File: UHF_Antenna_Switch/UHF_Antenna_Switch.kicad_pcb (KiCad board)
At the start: 2 copper layers, 157.2 x 60 mm, 47 parts, among them J1 Conn_N_Type_Female, J2 Conn_SO-239, J3 Conn_SMA_Female, J4 Screw_Terminal_01x04, J5 Conn_02x03_Odd_Even, K1 HF3-51, K2 HF3-51, Q2 2N7002, Q3 2N7002, SW1 SW_SP3T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

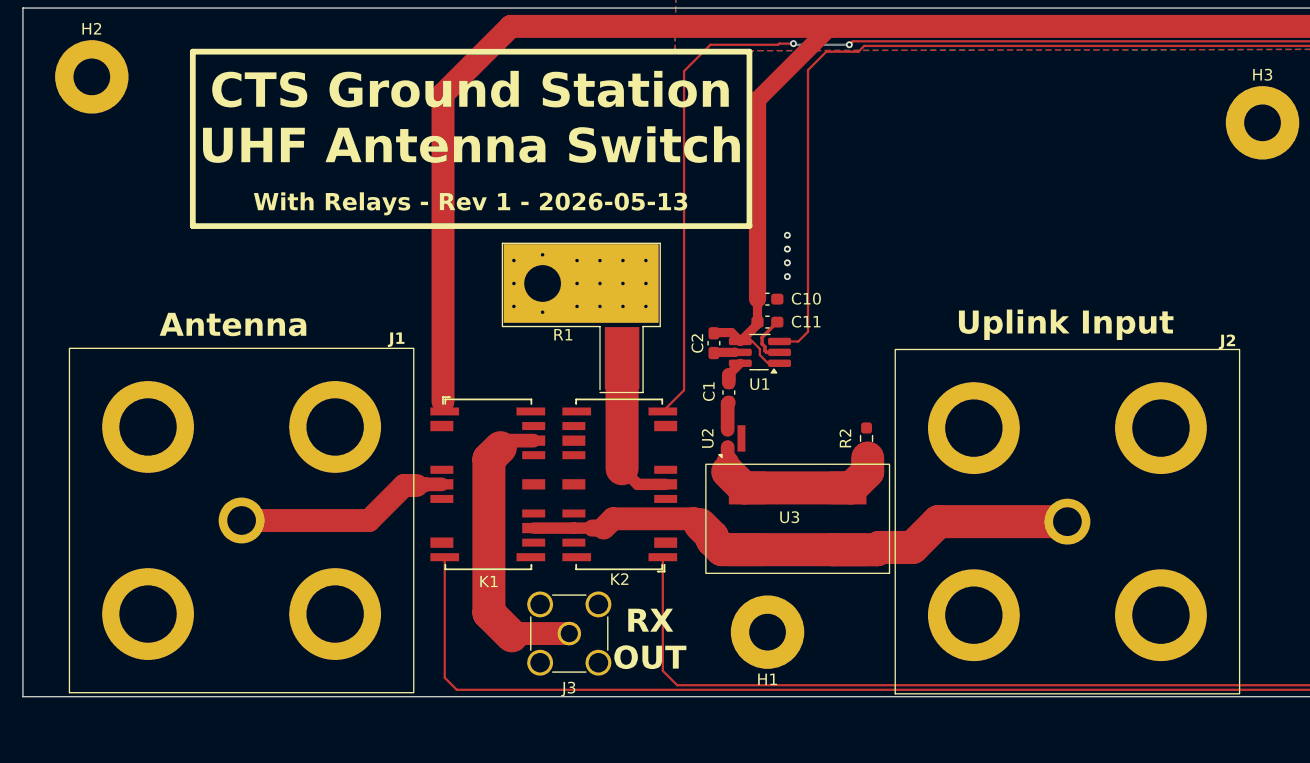
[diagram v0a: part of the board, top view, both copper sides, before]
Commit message: chore(pcb): Minor layout tweaks in RF area
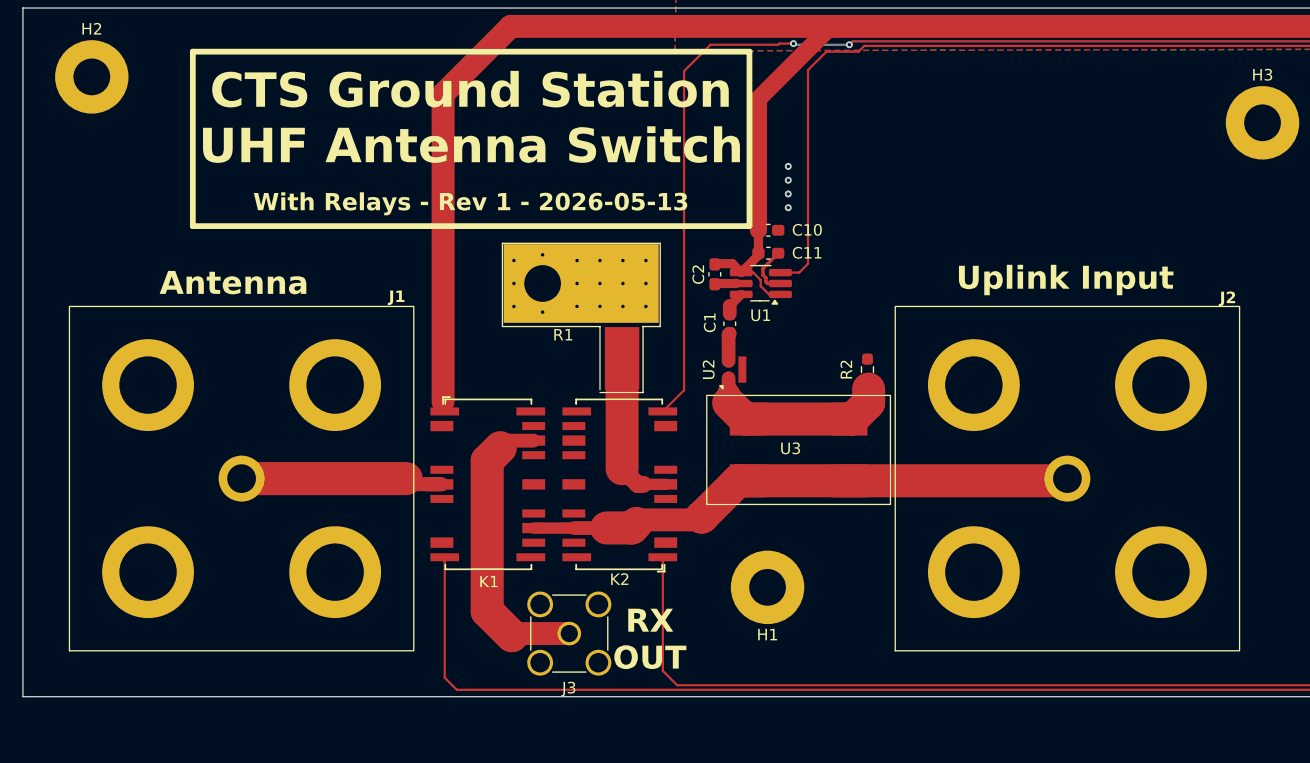
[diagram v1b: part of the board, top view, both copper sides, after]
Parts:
- moved C1 6.00 mm to (136.6, 102.5)
- moved C10 6.00 mm to (139.9, 94.4)
- moved C11 6.00 mm to (139.9, 96.4)
- moved C2 6.00 mm to (135.3, 98.2)
- moved R2 6.00 mm to (148.6, 106.5)
- moved U1 6.00 mm to (139.3, 99.0)
- moved U2 6.00 mm to (137.1, 106.5)
- moved U3 6.00 mm to (142.6, 114.8)
- moved H1 3.90 mm to (139.9, 125.5)
- moved J2 3.75 mm to (166.0, 116.0)
- moved J1 3.65 mm to (94.0, 116.0)
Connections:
- net /Relay_K1/RF_COMMON renamed /RF_PORT_ANT
- net /Relay_K1/RF_NC renamed /RF_PORT_RX
- net Net-(J2-In) renamed /RF_PORT_TX
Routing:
- net TX_DETECTED: track 135.1 -> 129.1 mm
- net +3V3: track 423.7 -> 417.8 mm
- net /RF_PORT_TX: track 21.5 -> 20.5 mm
- net /RF_PORT_ANT: track 18.1 -> 19.1 mm
- net /Relay_K1/RF_NO: track 22.6 -> 21.8 mm

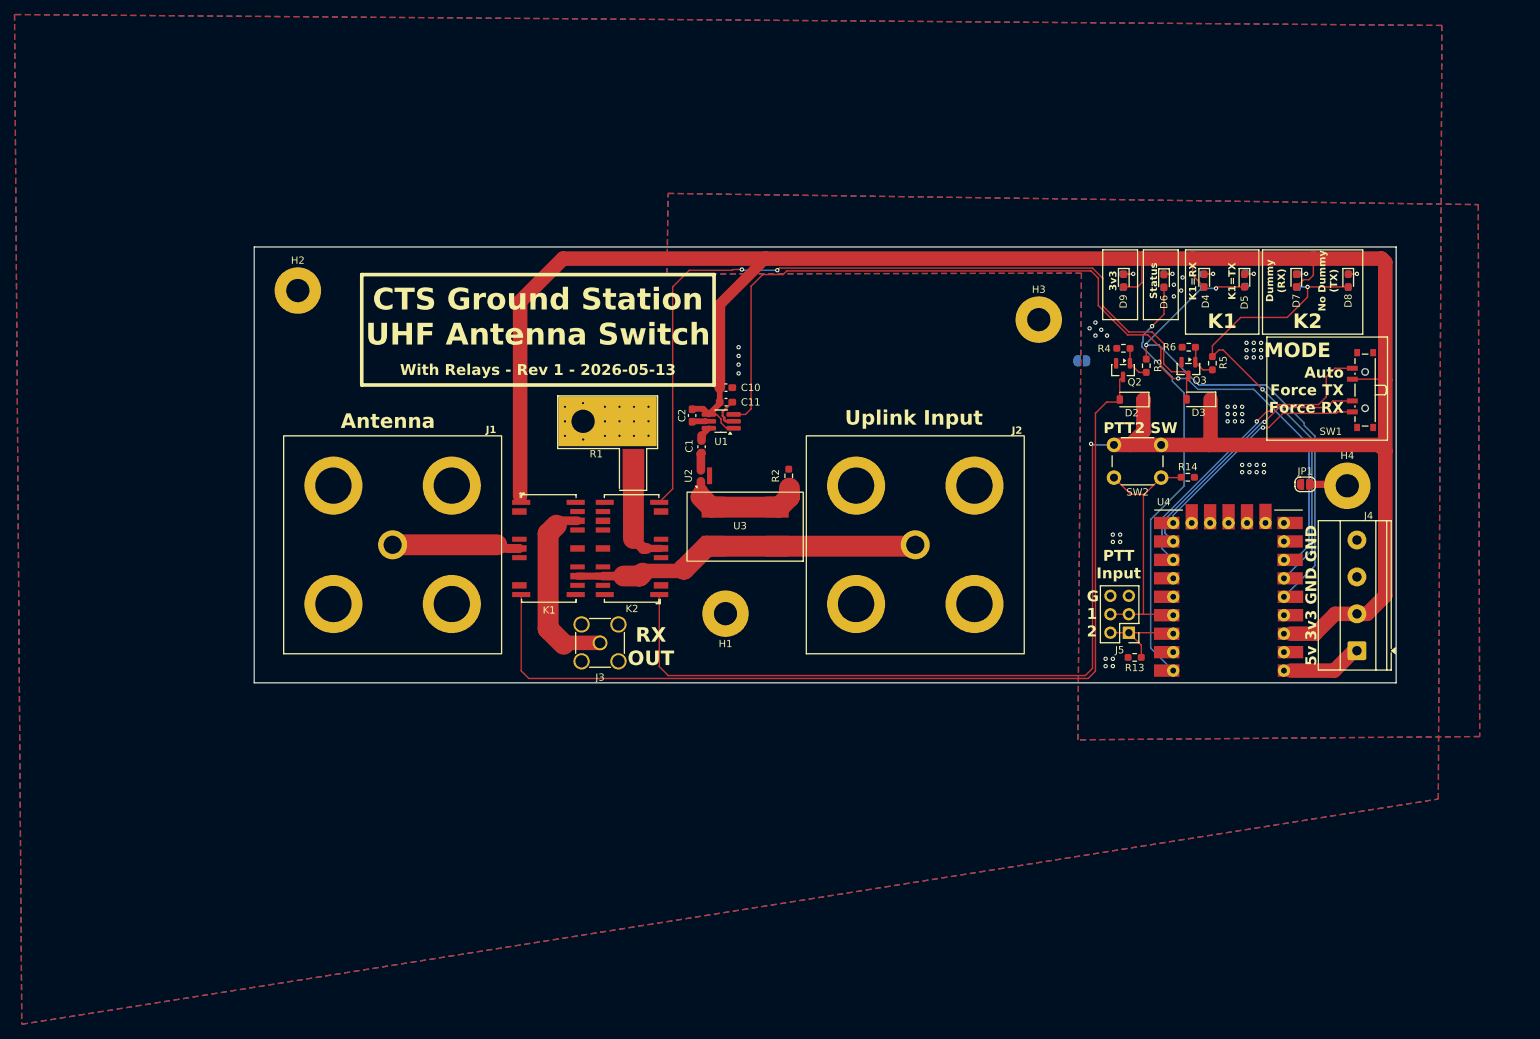
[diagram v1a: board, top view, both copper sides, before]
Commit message: feat(pcb): Add tons of fencing vias
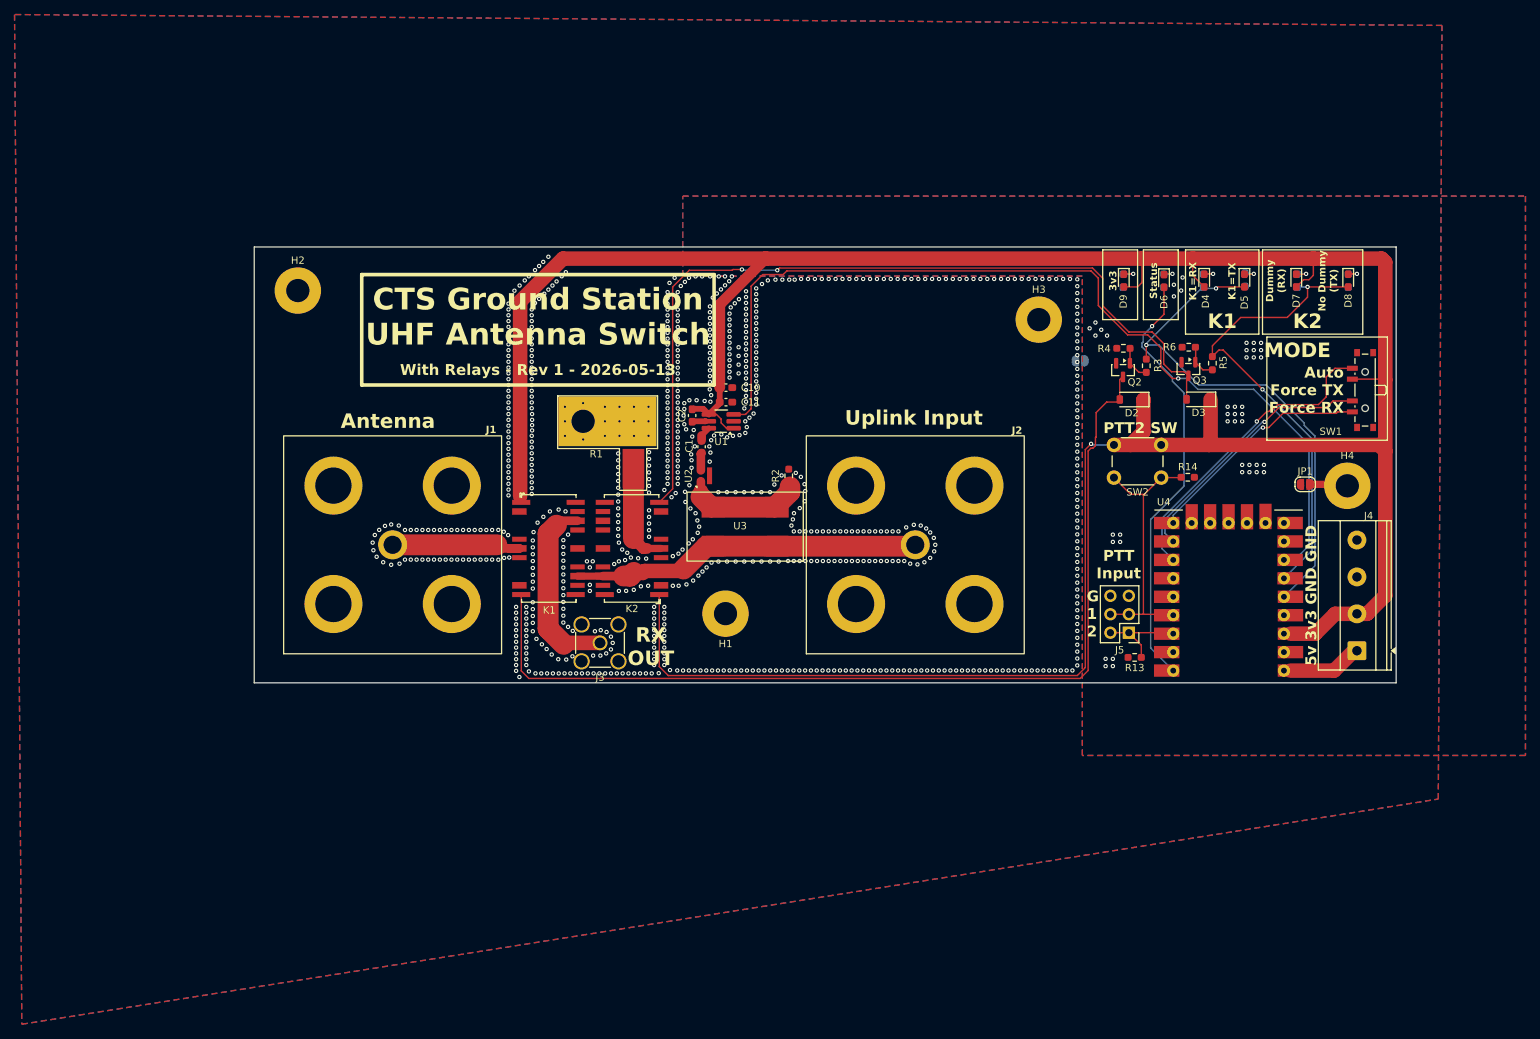
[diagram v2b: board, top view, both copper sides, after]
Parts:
- moved JP2 0.23 mm to (188.7, 90.7)
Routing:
- net GNDS: track 4.47 -> 0.00 mm, vias 4 -> 761
- net /Relay_K1/RF_NO: track 21.8 -> 20.3 mm
- net +3V3: track 417.8 -> 416.9 mm

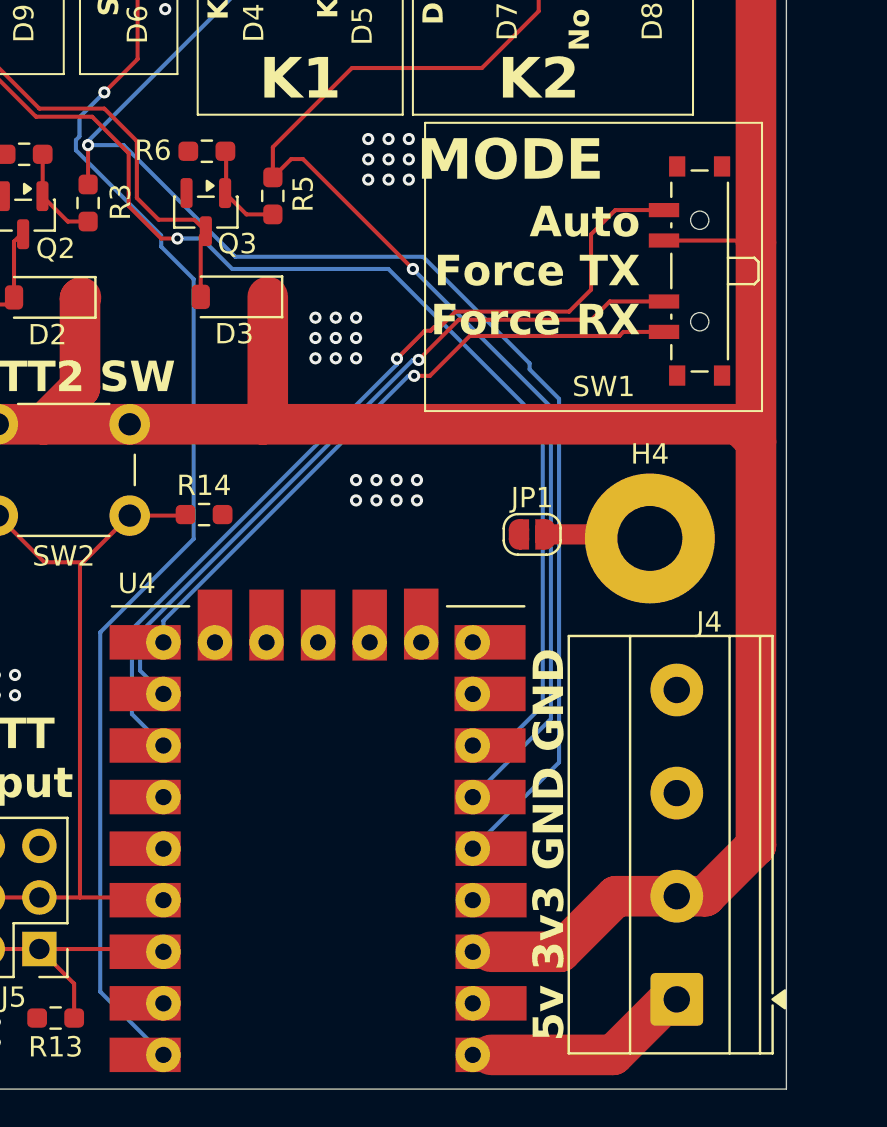
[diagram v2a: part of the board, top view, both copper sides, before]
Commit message: feat: Add Serial Override LED indicator
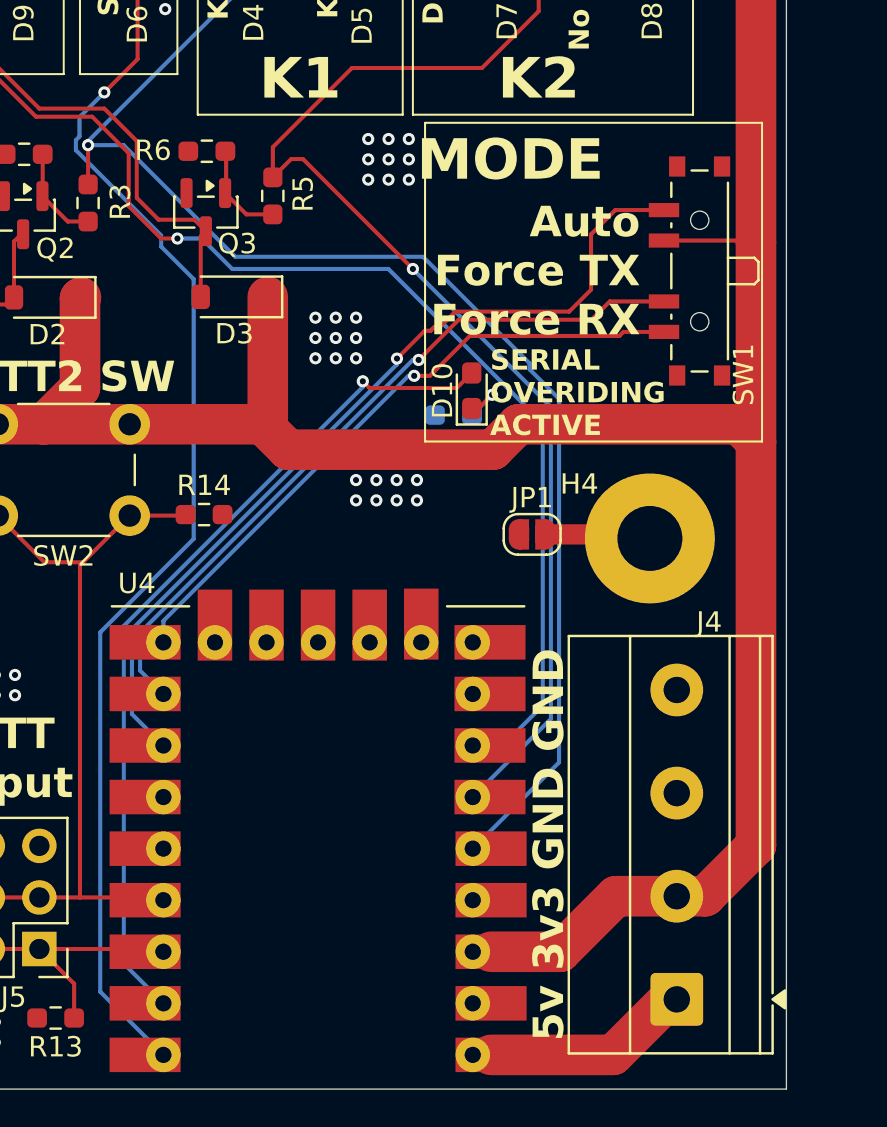
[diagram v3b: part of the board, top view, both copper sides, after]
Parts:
- added D10: LED, LED_SMD:LED_0603_1608Metric_Pad1.05x0.95mm_HandSolder, F.Cu at (216.7, 100.6)
- added R15: 3k9, Resistor_SMD:R_0603_1608Metric_Pad0.98x0.95mm_HandSolder, B.Cu at (215.8, 101.8)
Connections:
- U4 pad 11: unconnected-(U4-GP1-Pad11)_1 -> MODE_OVERRIDE_LED
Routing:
- net MODE_OVERRIDE_LED: track 0.00 -> 42.1 mm, vias 0 -> 1
- net Net-(D10-K): track 0.00 -> 2.69 mm, vias 0 -> 1
- net +3V3: track 416.9 -> 418.0 mm
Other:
- board text added: "SERIAL OVERIDING ACTIVE"

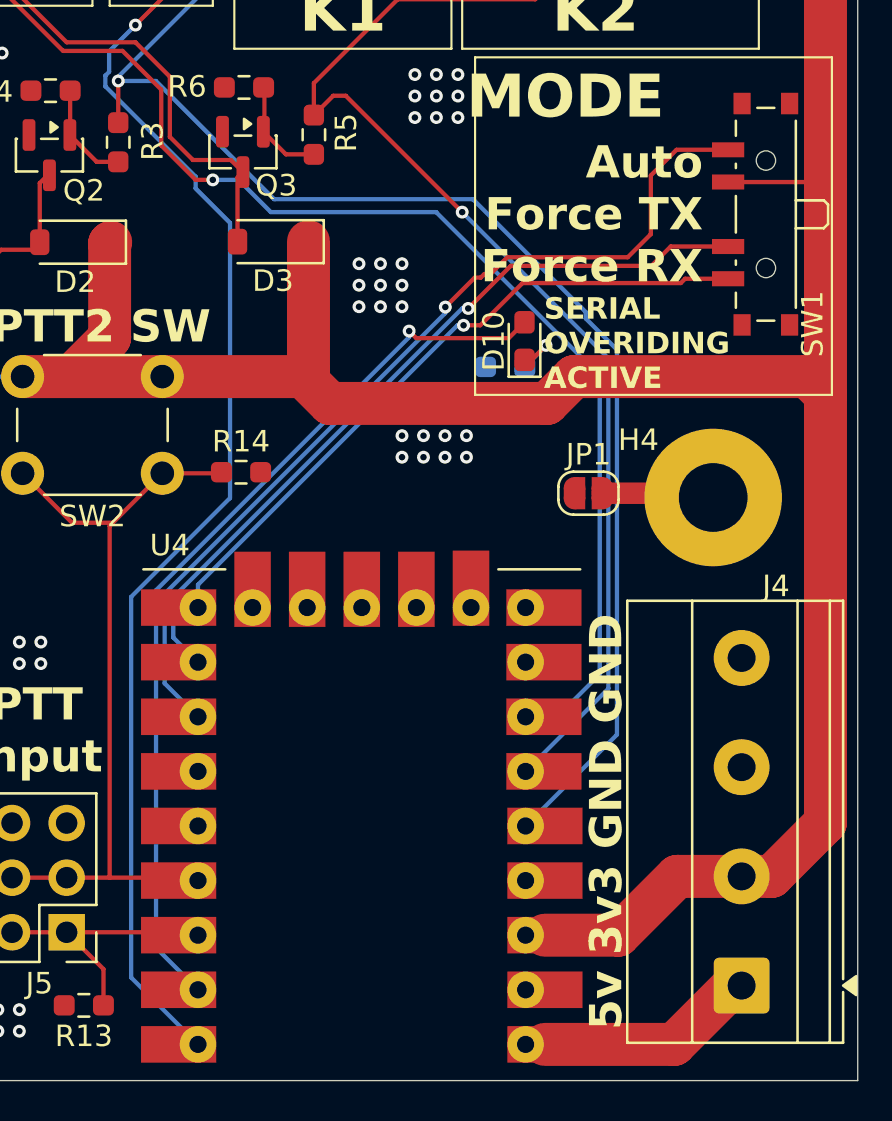
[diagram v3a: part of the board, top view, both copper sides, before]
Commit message: fix(pcb): Swap order of mode switch items
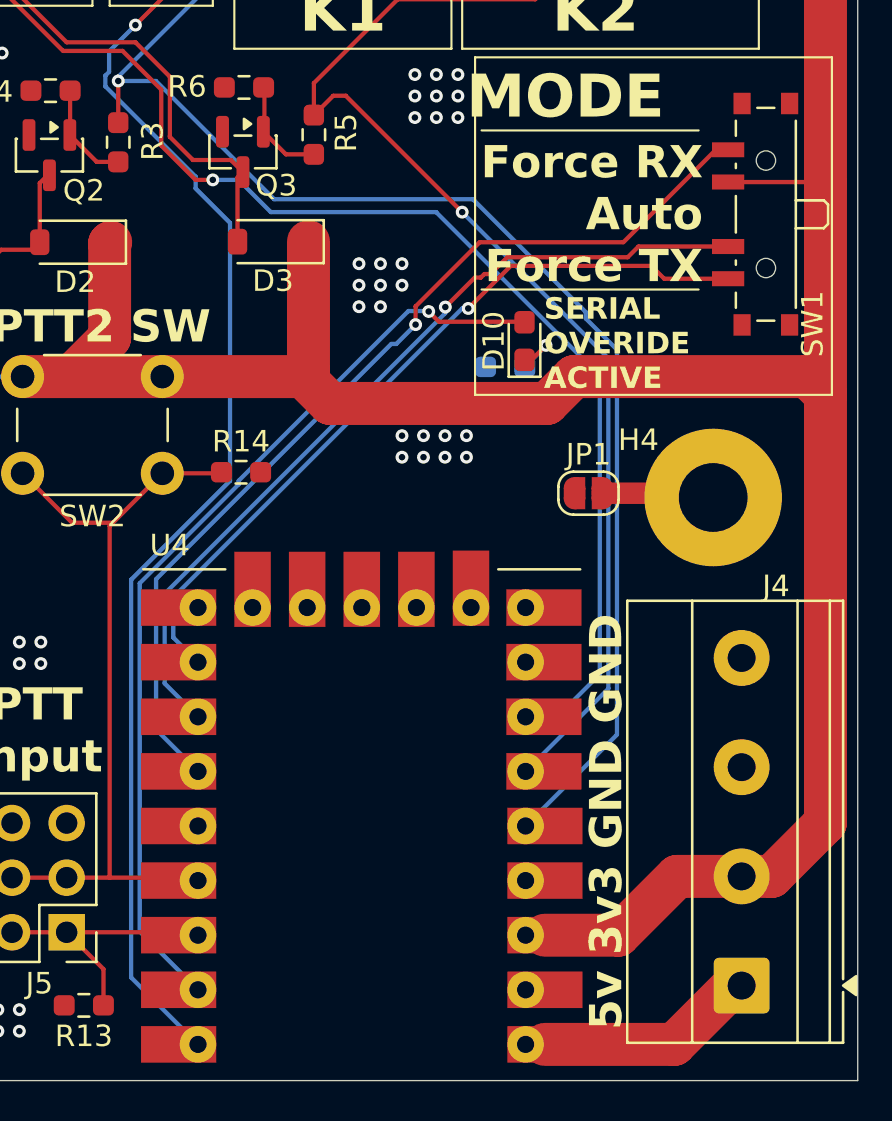
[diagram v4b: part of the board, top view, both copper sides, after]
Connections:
- SW1 pad 1: Net-(U4-GP8) -> Net-(U4-GP7)
- SW1 pad 2: Net-(U4-GP7) -> Net-(U4-GP6)
- SW1 pad 4: Net-(U4-GP6) -> Net-(U4-GP5)
- U4 pad 15: unconnected-(U4-GP5-Pad15) -> Net-(U4-GP5)
- U4 pad 18: Net-(U4-GP8) -> unconnected-(U4-GP8-Pad18)_1
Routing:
- net Net-(U4-GP5): track 0.00 -> 45.1 mm, vias 0 -> 1
- net Net-(U4-GP8): track 31.6 -> 0.00 mm, vias 1 -> 0
- net Net-(U4-GP6): track 42.9 -> 39.4 mm
- net MODE_OVERRIDE_LED: track 42.1 -> 43.5 mm
- net GNDD: vias 43 -> 42
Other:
- board text added: "Force RX Auto Force TX"
- board text added: "SERIAL OVERIDE ACTIVE"
- board text removed: "Auto Force TX Force RX"
- board text removed: "SERIAL OVERIDING ACTIVE"

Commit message: feat(pcb): Finish Rev 2 render, exports
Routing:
- net GNDS: vias 761 -> 778
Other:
- board text added: "CTS Ground Station T/R Antenna Switch"
- board text added: "UHF - Rev 2 - 2026-05-30"
- board text removed: "CTS Ground Station UHF Antenna Switch"
- board text removed: "With Relays - Rev 1 - 2026-05-13"
